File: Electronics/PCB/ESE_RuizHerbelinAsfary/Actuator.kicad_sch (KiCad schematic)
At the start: 0 parts

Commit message: added test pin
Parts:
- added C501: 1uF, symbol Device:C_Small
- added C502, C503, C504: C_Small, symbol Device:C_Small
- added J501, J502: Conn_01x06_Male, symbol Connector:Conn_01x06_Male
- added J503: Conn_01x03_Male, symbol Connector:Conn_01x03_Male
- added U501, U502: ZXBM5210-S, Package_SO:SOIC-8_3.9x4.9mm_P1.27mm, symbol Driver_Motor:ZXBM5210-S
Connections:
- new net: J502.1 (Pin_1), U502.1 (OUT1)
- new net: C504.1, U502.2 (VM)
- new net: J502.6 (Pin_6), U502.7 (OUT2)
- new net: J501.1 (Pin_1), U501.1 (OUT1)
- new net: C503.1, U501.2 (VM)
- new net: J501.6 (Pin_6), U501.7 (OUT2)
- new net +5V: J501.5 (Pin_5), J502.5 (Pin_5)
- new net +BATT: C501.1, C502.1, J503.2 (Pin_2), U501.3 (VDD), U501.6 (VREF), U502.3 (VDD), U502.6 (VREF)
- new net EncoderA_Left: J501.3 (Pin_3)
- new net EncoderA_Right: J502.3 (Pin_3)
- new net EncoderB_Left: J501.4 (Pin_4)
- new net EncoderB_Right: J502.4 (Pin_4)
- new net FWD_LeftMotor_PWM: U501.4 (FWD)
- new net FWD_RightMotor_PWM: U502.4 (FWD)
- new net GND: C501.2, C502.2, C503.2, C504.2, J501.2 (Pin_2), J502.2 (Pin_2), J503.1 (Pin_1), U501.8 (GND), U502.8 (GND)
- new net REV_LeftMotor_PWM: U501.5 (REV)
- new net REV_RightMotor_PWM: U502.5 (REV)
- new net UART_Servomoteur: J503.3 (Pin_3)
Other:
- note added: "Bloc Actionneur"
- note added: "Driver moteurs"
- note added: "Les connecteurs du servo sont des jst."
- note added: "Les connecteurs moteurs sont des jst xh 2A"
- note added: "Motor+"
- note added: "Motor-"
- note added: "Servomoteur"
- company: (none) -> ENSEA
- title: (none) -> Actuators

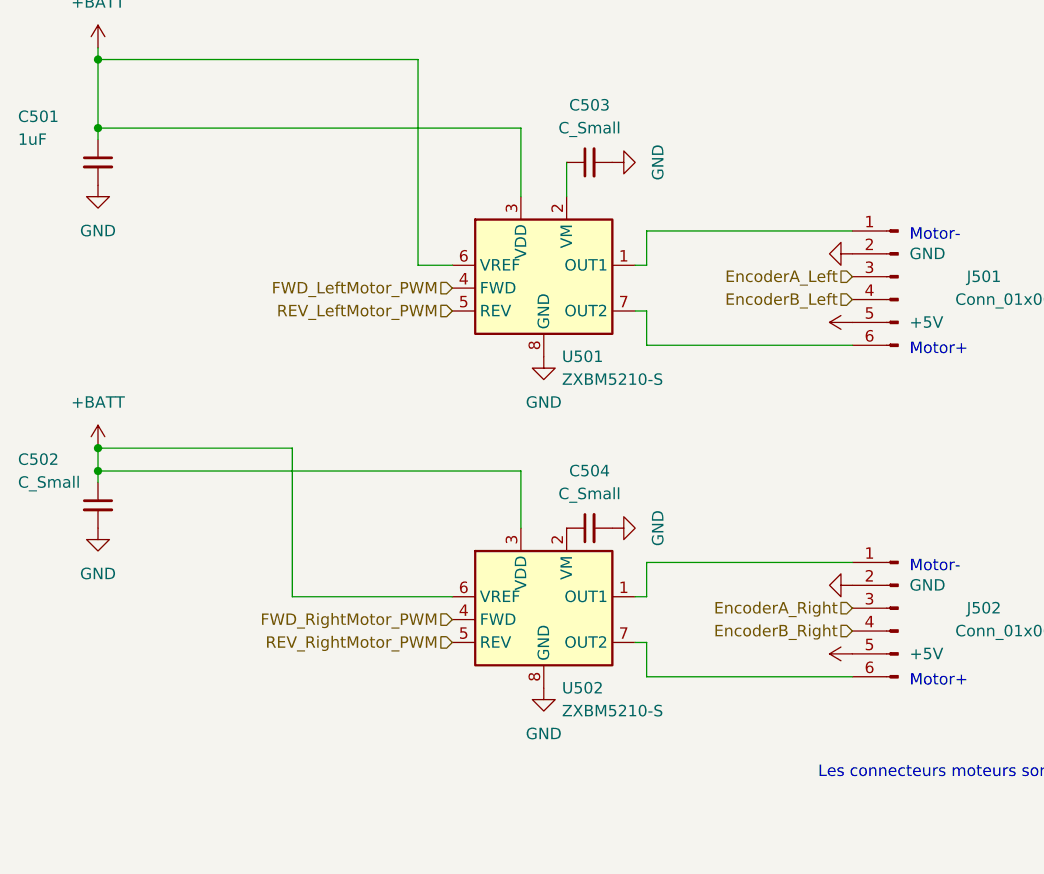
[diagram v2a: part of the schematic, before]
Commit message: added solderbridge before and after the driver
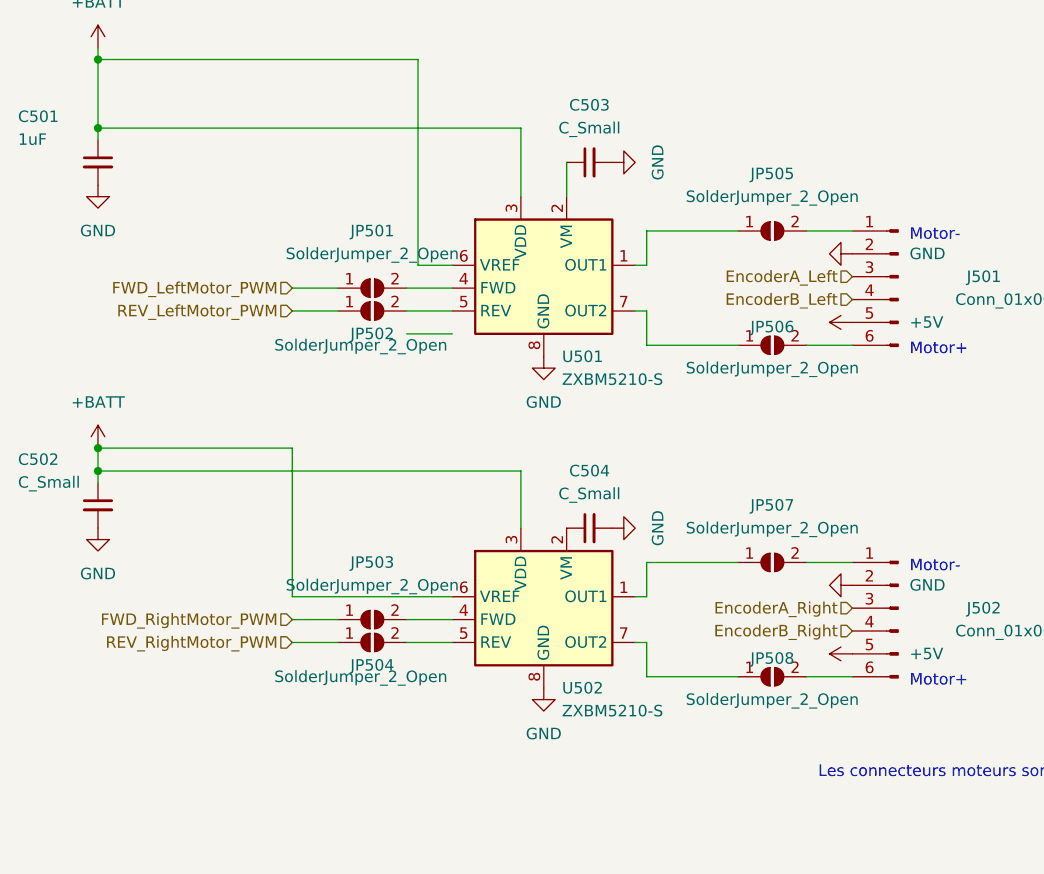
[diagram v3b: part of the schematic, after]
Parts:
- added JP501, JP502, JP503, JP504, JP505, JP506, JP507, JP508: SolderJumper_2_Open, symbol Jumper:SolderJumper_2_Open
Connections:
- net FWD_LeftMotor_PWM: now also JP501.1 (A); no longer U501.4 (FWD)
- net FWD_RightMotor_PWM: now also JP503.1 (A); no longer U502.4 (FWD)
- net REV_LeftMotor_PWM: now also JP502.1 (A); no longer U501.5 (REV)
- net REV_RightMotor_PWM: now also JP504.1 (A); no longer U502.5 (REV)
- net at U502.1 (OUT1): now also JP507.1 (A); no longer J502.1 (Pin_1)
- net at U502.7 (OUT2): now also JP508.1 (A); no longer J502.6 (Pin_6)
- net at U501.1 (OUT1): now also JP505.1 (A); no longer J501.1 (Pin_1)
- net at U501.7 (OUT2): now also JP506.1 (A); no longer J501.6 (Pin_6)
- new net: JP503.2 (B), U502.4 (FWD)
- new net: JP504.2 (B), U502.5 (REV)
- new net: J502.1 (Pin_1), JP507.2 (B)
- new net: J502.6 (Pin_6), JP508.2 (B)
- new net: JP502.2 (B), U501.5 (REV)
- new net: JP501.2 (B), U501.4 (FWD)
- new net: J501.1 (Pin_1), JP505.2 (B)
- new net: J501.6 (Pin_6), JP506.2 (B)
